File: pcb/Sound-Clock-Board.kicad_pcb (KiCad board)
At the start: 2 copper layers, 61 x 68.6 mm, 9 parts, among them J1 ESPThingLeftSide, J2 ESPThingRightSide, J3 I2SBoard, J4 ToConfigBtn, J5 ToTouchPlate

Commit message: Updated the pcb and the gcode files because the origin was wrong.
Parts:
- moved J1 211.6 mm to (-51.0, -51.0)
- moved J2 211.6 mm to (-25.6, -51.0)
- moved J3 211.6 mm to (-12.9, -30.7)
- moved J4 211.6 mm to (-12.9, -12.9)
- moved J5 211.6 mm to (-12.9, -20.5)
- moved REF** 211.6 mm to (-56.1, -5.28)
- moved REF** 211.6 mm to (-5.28, -5.28)
- moved REF** 211.6 mm to (-56.1, -63.7)
- moved REF** 211.6 mm to (-5.28, -63.7)

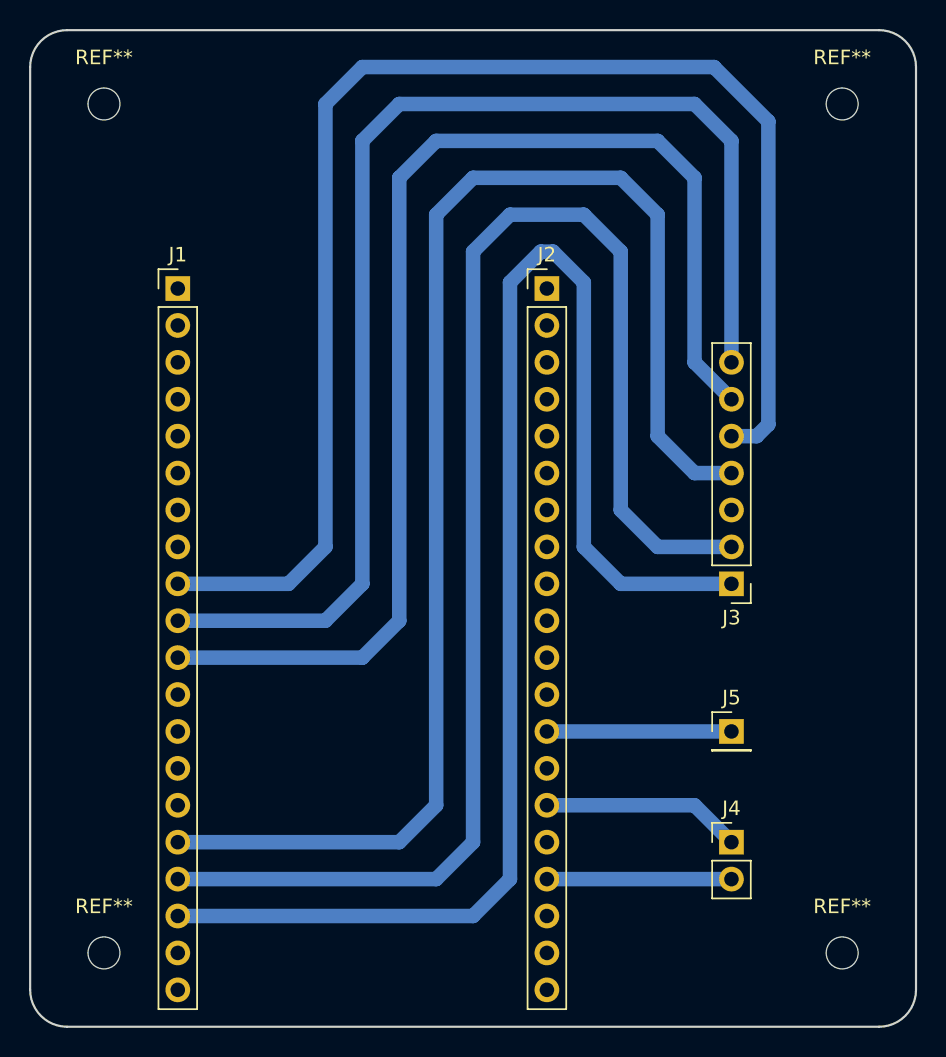
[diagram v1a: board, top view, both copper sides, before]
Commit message: Updated PCB.
The radio  isn't working right when it's plugged into the board, so there's a problem on this simple board somewhere.
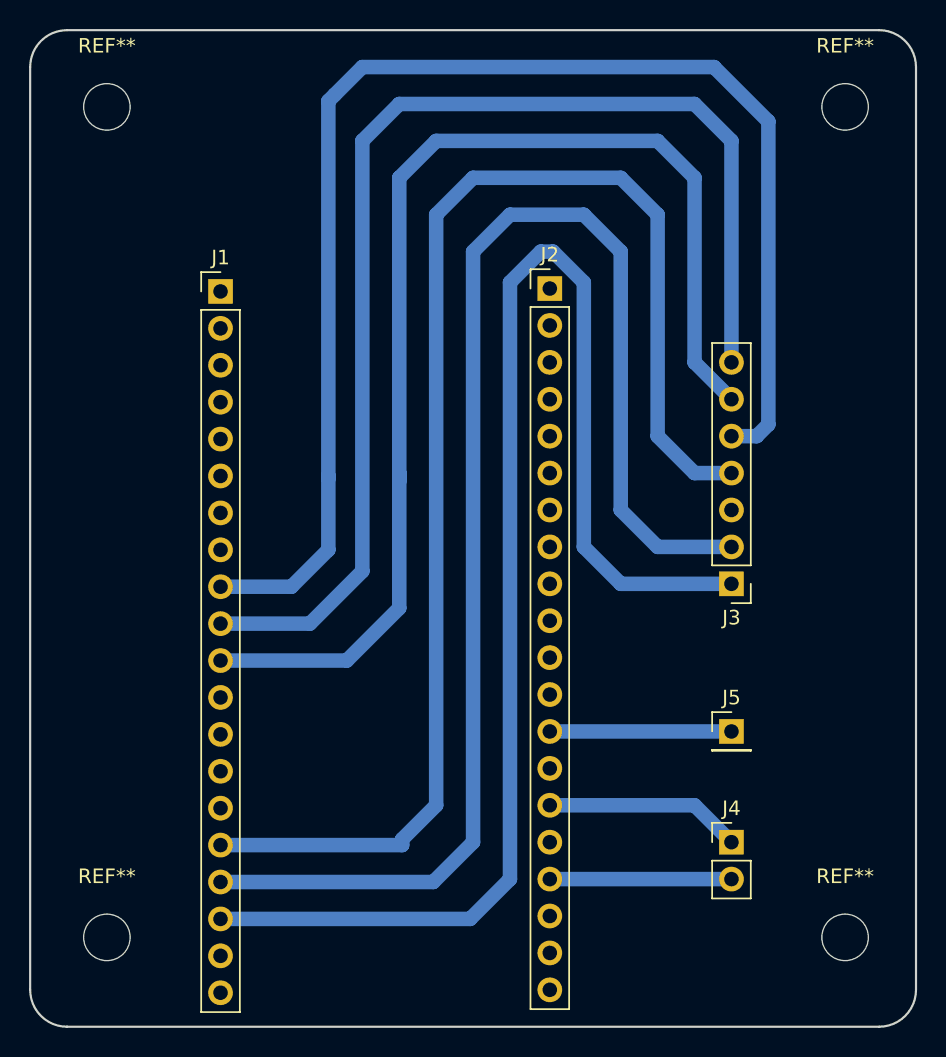
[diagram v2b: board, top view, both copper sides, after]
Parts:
- removed the REF** at (-56.1, -5.28)
- removed the REF** at (-5.28, -5.28)
- removed the REF** at (-56.1, -63.7)
- removed the REF** at (-5.28, -63.7)
- added REF**: MountingHole_3.2mm_M3, MountingHole:MountingHole_3.2mm_M3, F.Cu at (-5.08, -6.35)
- added REF**: MountingHole_3.2mm_M3, MountingHole:MountingHole_3.2mm_M3, F.Cu at (-55.9, -6.35)
- added REF**: MountingHole_3.2mm_M3, MountingHole:MountingHole_3.2mm_M3, F.Cu at (-55.9, -63.5)
- added REF**: MountingHole_3.2mm_M3, MountingHole:MountingHole_3.2mm_M3, F.Cu at (-5.08, -63.5)
- moved J1 2.95 mm to (-48.1, -50.8)
- moved J2 0.20 mm to (-25.4, -51.0)
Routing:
- net Net-(J1-Pad10): track 87.1 -> 83.6 mm
- net Net-(J1-Pad18): track 101.2 -> 98.4 mm
- net Net-(J1-Pad17): track 100.7 -> 97.9 mm
- net Net-(J1-Pad11): track 85.5 -> 82.7 mm
- net Net-(J1-Pad16): track 98.2 -> 95.6 mm
- net Net-(J1-Pad9): track 98.5 -> 96.1 mm

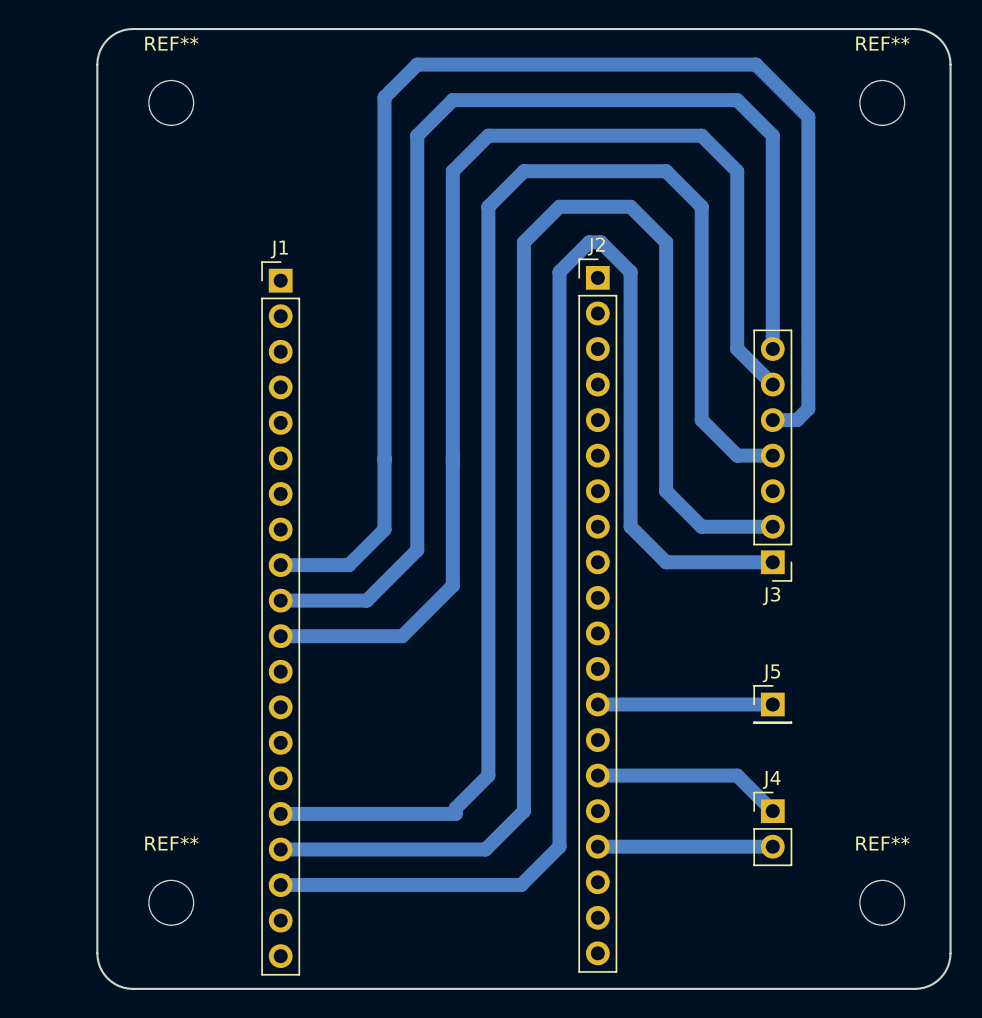
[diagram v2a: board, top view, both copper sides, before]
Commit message: Fixed an incorrect trace
I had a trace going to the VBAT pin that should have been going to VUSB.  Worked when not plugged in, or when in a breadboard, but didn't work on the circuit boards I milled.
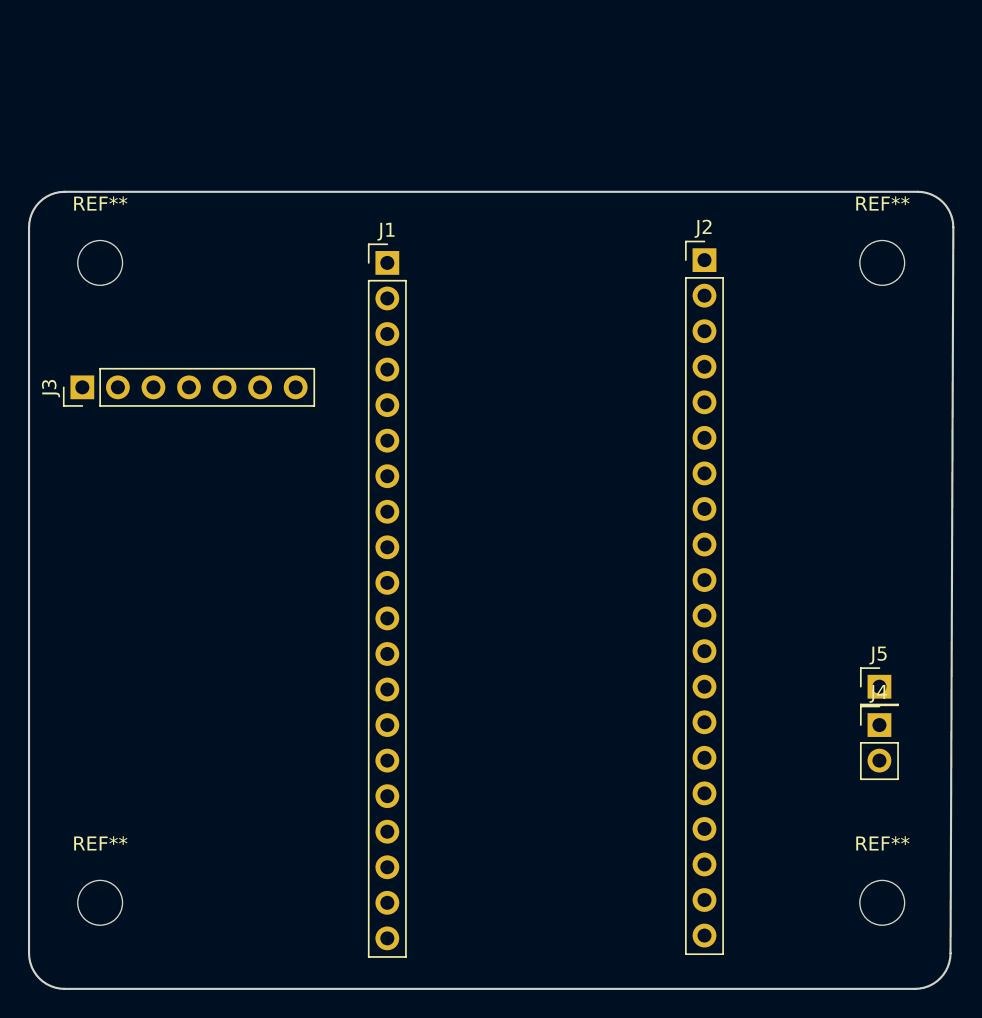
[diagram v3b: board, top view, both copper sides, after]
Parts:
- moved J3 50.9 mm to (-62.2, -43.2), turned to 90 degrees
- moved REF** 12.5 mm to (-61.0, -52.1)
- moved REF** 11.4 mm to (-5.08, -52.1)
- moved J4 9.79 mm to (-5.28, -19.1)
- moved J1 7.73 mm to (-40.4, -52.1)
- moved J5 7.73 mm to (-5.28, -21.8)
- moved J2 7.73 mm to (-17.8, -52.3)
- moved REF** 5.08 mm to (-61.0, -6.35)
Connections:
- J3 pad 1: Net-(J1-Pad18) -> Net-(J1-Pad19)
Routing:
- net Net-(J1-Pad18): track 98.4 -> 0.00 mm
- net Net-(J1-Pad17): track 97.9 -> 0.00 mm
- net Net-(J1-Pad9): track 96.1 -> 0.00 mm
- net Net-(J1-Pad16): track 95.6 -> 0.00 mm
- net Net-(J1-Pad10): track 83.6 -> 0.00 mm
- net Net-(J1-Pad11): track 82.7 -> 0.00 mm
- net Net-(J2-Pad15): track 13.8 -> 0.00 mm
- net Net-(J2-Pad17): track 12.7 -> 0.00 mm
- net Net-(J2-Pad13): track 12.7 -> 0.00 mm
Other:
- board size 61 x 68.6 mm -> 66 x 57 mm

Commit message: Added gain control and merged the single pin header with the two pin header for strength
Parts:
- removed J5: ToTouchPlate, Connector_PinHeader_2.54mm:PinHeader_1x01_P2.54mm_Vertical
- added R1: R_Small_US, Resistor_THT:R_Axial_DIN0207_L6.3mm_D2.5mm_P2.54mm_Vertical, F.Cu at (-44.5, -19.1)
- J4: value ToConfigBtn -> Touch sensor and config switch; footprint Connector_PinHeader_2.54mm:PinHeader_1x02_P2.54mm_Vertical -> Connector_PinHeader_2.54mm:PinHeader_1x03_P2.54mm_Vertical
- moved J3 14.0 mm to (-48.3, -43.2), turned to 0 degrees
- moved J4 5.50 mm to (-10.2, -21.6)
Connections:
- J3 pad 1: Net-(J1-Pad19) -> Net-(J1-Pad16)
- J3 pad 4: Net-(J1-Pad16) -> Net-(J1-Pad14)
- J4 pad 1: Net-(J2-Pad15) -> Net-(J2-Pad13)
- J4 pad 2: Net-(J2-Pad17) -> Net-(J2-Pad15)
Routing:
- net Net-(J1-Pad17): track 0.00 -> 66.9 mm
- net Net-(J1-Pad16): track 0.00 -> 49.6 mm
- net Net-(J1-Pad14): track 0.00 -> 34.1 mm
- net Net-(J1-Pad11): track 0.00 -> 21.4 mm
- net Net-(J2-Pad17): track 0.00 -> 9.64 mm
- net Net-(J2-Pad15): track 0.00 -> 8.59 mm
- net Net-(J2-Pad13): track 0.00 -> 8.39 mm
- net Net-(J1-Pad9): track 0.00 -> 8.35 mm
- net Net-(J1-Pad10): track 0.00 -> 8.35 mm
- net Net-(J1-Pad13): track 0.00 -> 4.01 mm
